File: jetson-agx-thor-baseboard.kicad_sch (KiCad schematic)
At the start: 0 parts

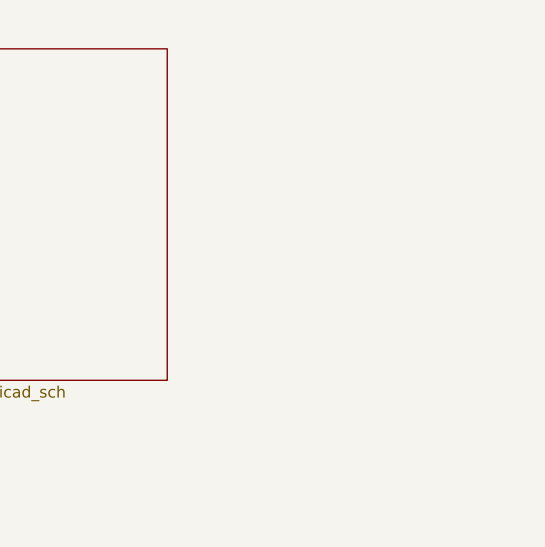
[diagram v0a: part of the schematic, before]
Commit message: [#82847] Prepare current state of schematic to merge with mockup
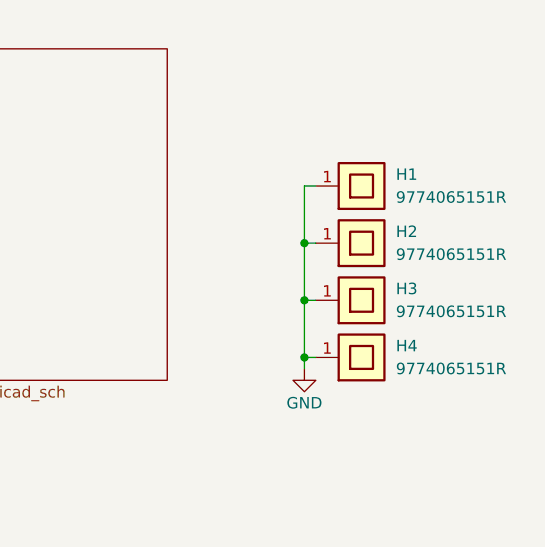
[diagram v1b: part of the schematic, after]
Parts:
- added H1, H2, H3, H4: Spacer_Drill3.7mm_H6.5mm_9774065151R, antmicro-footprints:Spacer_Drill3.7mm_H6.5mm_9774065151R, symbol antmicroMechanicalParts:Spacer_Drill3.7mm_H6.5mm_9774065151R
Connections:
- new net GND: H1.1, H2.1, H3.1, H4.1

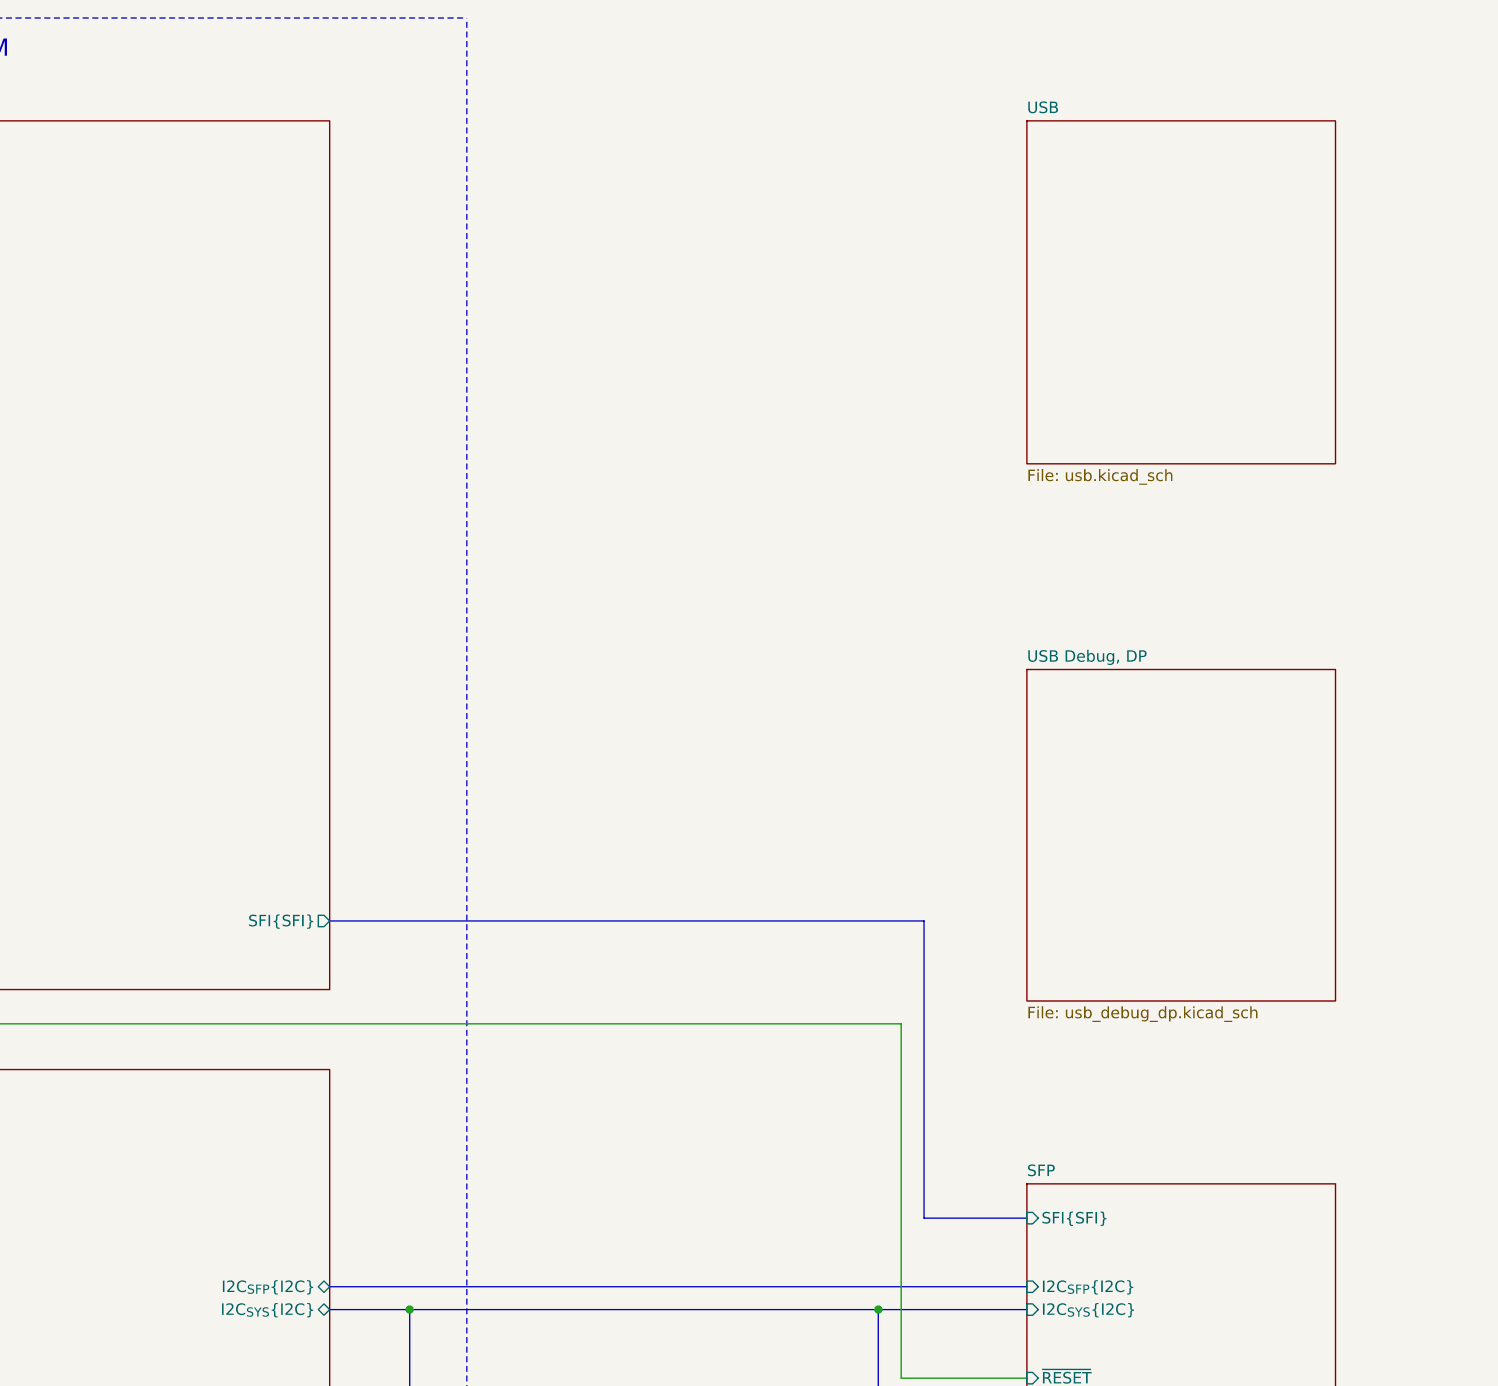
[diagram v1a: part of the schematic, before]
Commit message: [#82837] Reorganize project: split each USB subsheet into two subsheets
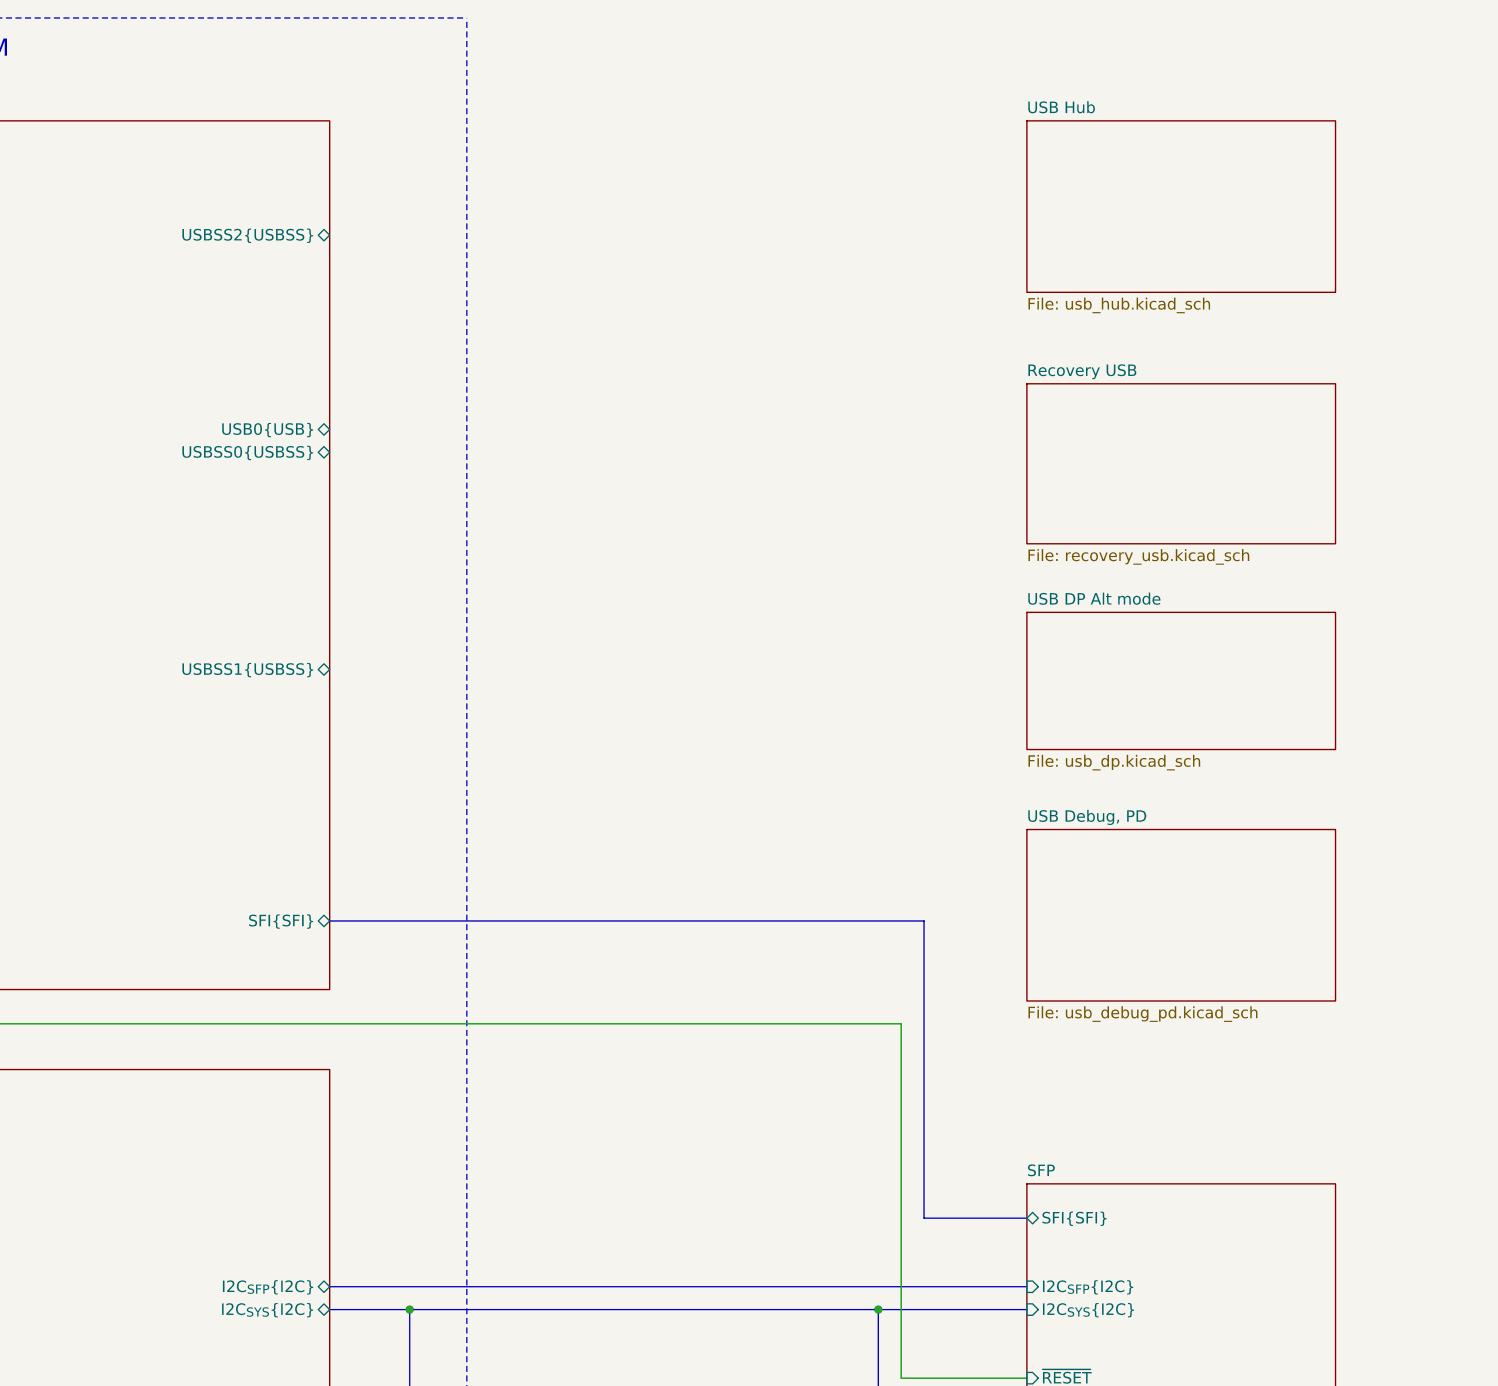
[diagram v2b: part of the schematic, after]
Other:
- sheet USB renamed USB Hub
- sheet USB Debug, DP renamed USB Debug, PD
- added sheet Recovery USB (recovery_usb.kicad_sch)
- added sheet USB DP Alt mode (usb_dp.kicad_sch)
- sheet SoM_IO2 ports: added USB0{USB}, USBSS0{USBSS}, USBSS1{USBSS}, USBSS2{USBSS}; removed none
- sheet USB Debug, PD: file usb_debug_dp.kicad_sch -> usb_debug_pd.kicad_sch
- sheet USB Hub: file usb.kicad_sch -> usb_hub.kicad_sch
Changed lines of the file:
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@@
 		(comment 1 "www.antmicro.com")
+	)
+	(bus_alias "USBSS"
+		(members "TX+" "TX-" "RX+" "RX-")
 	)
 	(text "SoM\n"
@@
 	)
 	(sheet
-		(at 331.47 93.98)
-		(size 34.29 36.83)
+		(at 331.47 111.76)
+		(size 34.29 19.05)
 		(exclude_from_sim no)
 		(in_bom yes)
@@
 			(color 0 0 0 0.0000)
 		)
-		(property "Sheetname" "USB Debug, DP"
-			(at 331.47 93.2684 0)
-			(effects
-				(font
-					(size 1.27 1.27)
-				)
-				(justify left bottom)
-			)
-		)
-		(property "Sheetfile" "usb_debug_dp.kicad_sch"
+		(property "Sheetname" "USB Debug, PD"
+			(at 331.47 111.0484 0)
+			(effects
+				(font
+					(size 1.27 1.27)
+				)
+				(justify left bottom)
+			)
+		)
+		(property "Sheetfile" "usb_debug_pd.kicad_sch"
 			(at 331.47 131.3946 0)
 			(effects
@@
 			(project "jetson-agx-thor-baseboard"
 				(path "/f569b0be-0afd-48b7-93ee-28582a4c645c"
-					(page "8")
+					(page "10")
 				)
 			)
@@
 	(sheet
 		(at 331.47 33.02)
-		(size 34.29 38.1)
+		(size 34.29 19.05)
 		(exclude_from_sim no)
 		(in_bom yes)
@@
 			(color 0 0 0 0.0000)
 		)
-		(property "Sheetname" "USB"
+		(property "Sheetname" "USB Hub"
 			(at 331.47 32.3084 0)
 			(effects
@@
 			)
 		)
-		(property "Sheetfile" "usb.kicad_sch"
-			(at 331.47 71.7046 0)
+		(property "Sheetfile" "usb_hub.kicad_sch"
+			(at 331.47 52.6546 0)
 			(effects
 				(font
@@
 			(project "jetson-agx-thor-baseboard"
 				(path "/f569b0be-0afd-48b7-93ee-28582a4c645c"
-					(page "11")
+					(page "13")
 				)
 			)
@@
 			(project "jetson-agx-thor-baseboard"
 				(path "/f569b0be-0afd-48b7-93ee-28582a4c645c"
-					(page "9")
+					(page "11")
 				)
 			)
@@
 			(project "jetson-agx-thor-baseboard"
 				(path "/f569b0be-0afd-48b7-93ee-28582a4c645c"
-					(page "13")
+					(page "15")
 				)
 			)
@@
 			)
 		)
-		(pin "SFI{SFI}" output
+		(pin "SFI{SFI}" bidirectional
 			(at 254 121.92 0)
 			(effects
@@
 				)
 				(justify left)
+			)
+		)
+		(pin "USB0{USB}" bidirectional
+			(at 254 67.31 0)
+			(effects
+				(font
+					(size 1.27 1.27)
+				)
+				(justify right)
+			)
+		)
+		(pin "USBSS0{USBSS}" bidirectional
+			(at 254 69.85 0)
+			(effects
+				(font
+					(size 1.27 1.27)
+				)
+				(justify right)
+			)
+		)
+		(pin "USBSS1{USBSS}" bidirectional
+			(at 254 93.98 0)
+			(effects
+				(font
+					(size 1.27 1.27)
+				)
+				(justify right)
+			)
+		)
+		(pin "USBSS2{USBSS}" bidirectional
+			(at 254 45.72 0)
+			(effects
+				(font
+					(size 1.27 1.27)
+				)
+				(justify right)
 			)
 		)
@@
 				(path "/f569b0be-0afd-48b7-93ee-28582a4c645c"
 					(page "3")
+				)
+			)
+		)
+	)
+	(sheet
+		(at 331.47 87.63)
+		(size 34.29 15.24)
+		(exclude_from_sim no)
+		(in_bom yes)
+		(on_board yes)
+		(dnp no)
+		(fields_autoplaced yes)
+		(stroke
+			(width 0.1524)
+			(type solid)
+		)
+		(fill
+			(color 0 0 0 0.0000)
+		)
+		(property "Sheetname" "USB DP Alt mode"
+			(at 331.47 86.9184 0)
+			(effects
+				(font
+					(size 1.27 1.27)
+				)
+				(justify left bottom)
+			)
+		)
+		(property "Sheetfile" "usb_dp.kicad_sch"
+			(at 331.47 103.4546 0)
+			(effects
+				(font
+					(size 1.27 1.27)
+				)
+				(justify left top)
+			)
+		)
+		(instances
+			(project "jetson-agx-thor-baseboard"
+				(path "/f569b0be-0afd-48b7-93ee-28582a4c645c"
+					(page "9")
 				)
 			)
@@
 			)
 		)
-		(pin "SFI{SFI}" input
+		(pin "SFI{SFI}" bidirectional
 			(at 331.47 154.94 180)
 			(effects
@@
 			(project "jetson-agx-thor-baseboard"
 				(path "/f569b0be-0afd-48b7-93ee-28582a4c645c"
-					(page "10")
+					(page "12")
+				)
+			)
+		)
+	)
+	(sheet
+		(at 331.47 62.23)
+		(size 34.29 17.78)
+		(exclude_from_sim no)
+		(in_bom yes)
+		(on_board yes)
+		(dnp no)
+		(fields_autoplaced yes)
+		(stroke
+			(width 0.1524)
+			(type solid)
+		)
+		(fill
+			(color 0 0 0 0.0000)
+		)
+		(property "Sheetname" "Recovery USB"
+			(at 331.47 61.5184 0)
+			(effects
+				(font
+					(size 1.27 1.27)
+				)
+				(justify left bottom)
+			)
+		)
+		(property "Sheetfile" "recovery_usb.kicad_sch"
+			(at 331.47 80.5946 0)
+			(effects
+				(font
+					(size 1.27 1.27)
+				)
+				(justify left top)
+			)
+		)
+		(instances
+			(project "jetson-agx-thor-baseboard"
+				(path "/f569b0be-0afd-48b7-93ee-28582a4c645c"
+					(page "8")
 				)
 			)
@@
 			(project "jetson-agx-thor-baseboard"
 				(path "/f569b0be-0afd-48b7-93ee-28582a4c645c"
-					(page "12")
-				)
-			)
+					(page "14")
+				)
+			)

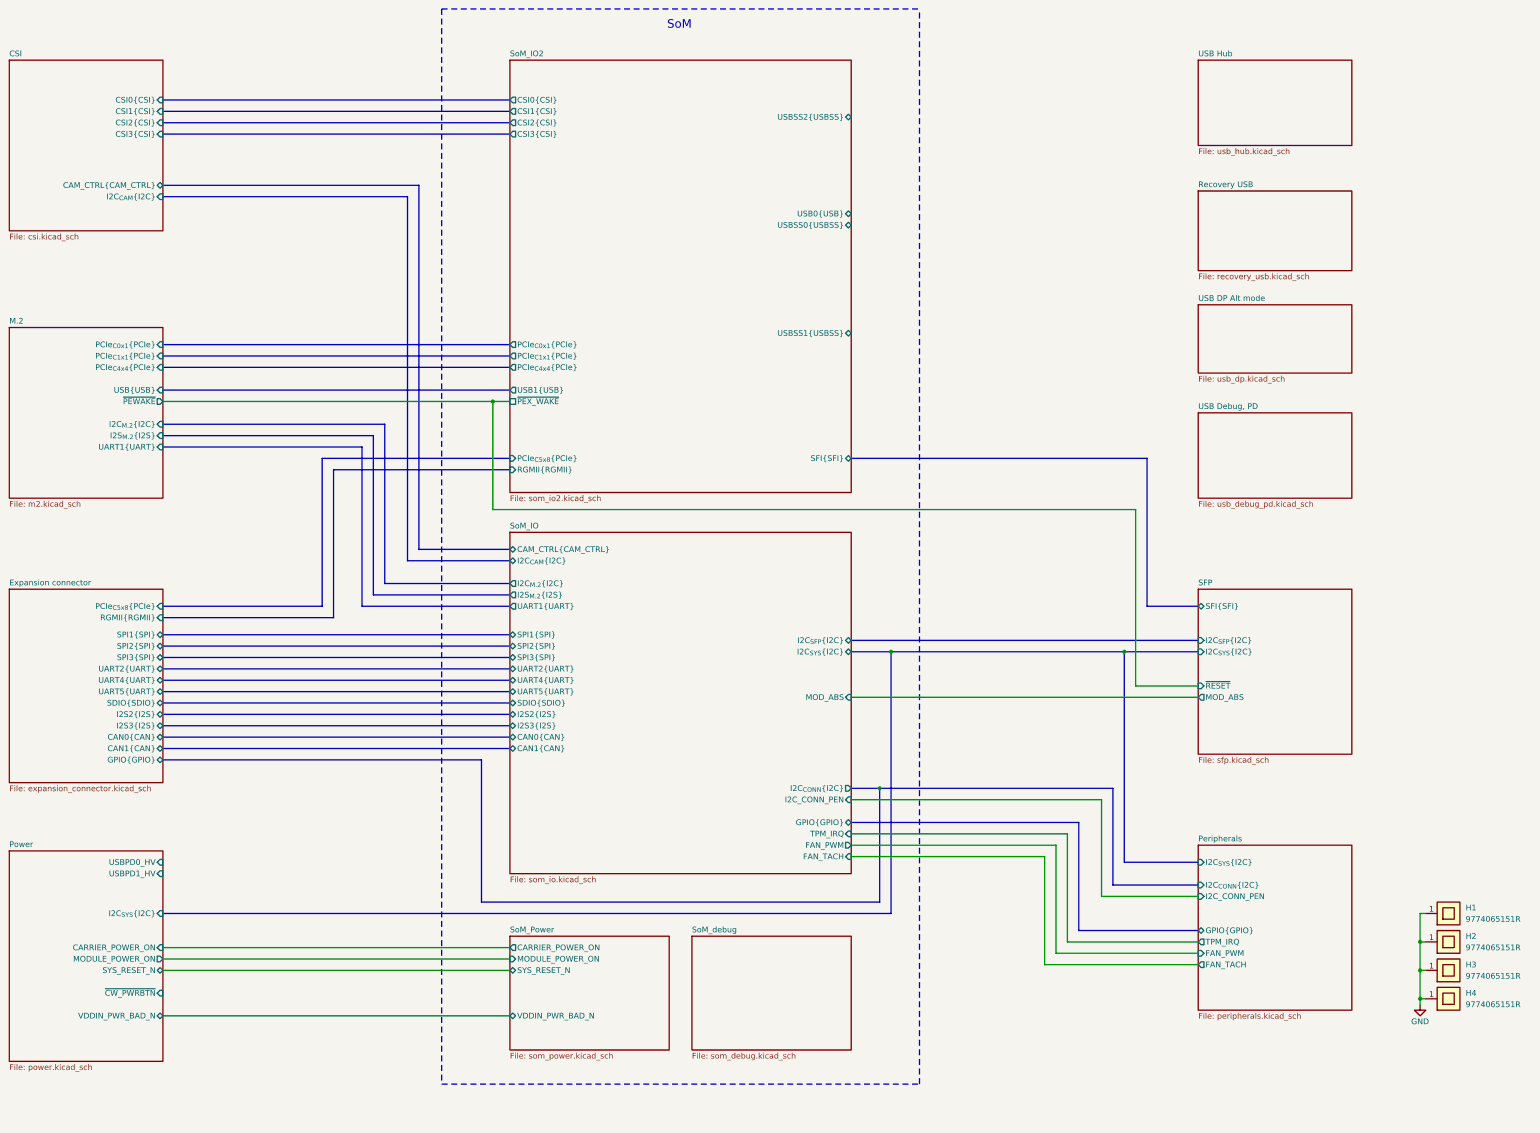
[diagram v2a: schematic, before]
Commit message: [#82837] Fix USB recovery and flashing section
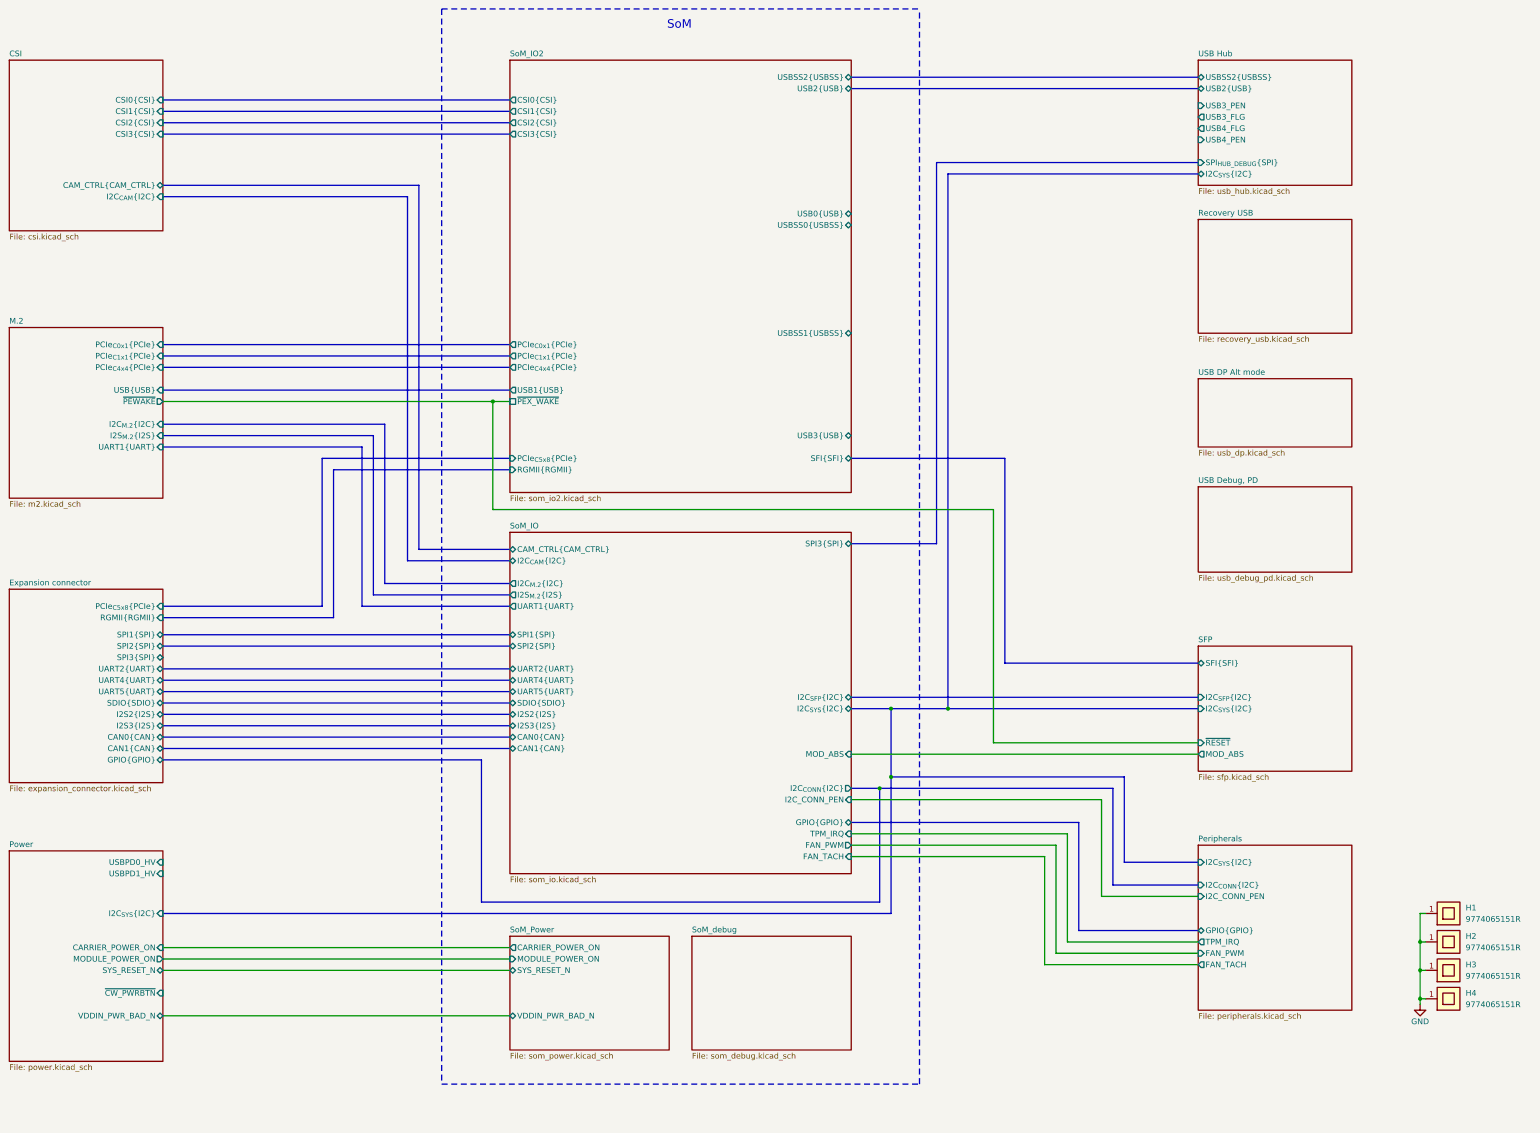
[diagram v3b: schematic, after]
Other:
- sheet SoM_IO2 ports: added USB2{USB}, USB3{USB}; removed none
- sheet USB Hub ports: added I2C_{SYS}{I2C}, SPI_{HUB_DEBUG}{SPI}, USB2{USB}, USB3_FLG, USB3_PEN, USB4_FLG, USB4_PEN, USBSS2{USBSS}; removed none
